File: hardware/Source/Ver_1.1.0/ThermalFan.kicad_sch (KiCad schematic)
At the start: 0 parts

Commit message: update pcb v1.1.0
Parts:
- added C35: 10uF, automative_hexapod:Ceramic_Cap_0805, symbol automative_hexapod:Ceramic_Cap_0805_10uF_16V
- added C36: 100nF, automative_hexapod:Ceramic_Cap_0805, symbol automative_hexapod:Ceramic_Cap_0805_100nF_50V
- added J5: Connector, automative_hexapod:JST-XH-SMD-2-2.54mm, symbol automative_hexapod:JST-XH-SMD-2-2.54mm
- added Q5: LN2302LT1G, automative_hexapod:SOT23, symbol automative_hexapod:LN2302LT1G
- added R36: 4.7Ohm, automative_hexapod:Res_0603, symbol automative_hexapod:Res_4.7_0603_1%
- added R37, R38: 10kOhm, automative_hexapod:Res_0603, symbol automative_hexapod:Res_10K_0603_1%
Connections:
- new net: Q5.1 (G), R36.2, R37.2
- new net: J5.1 (Pin_1), R38.1
- new net: J5.2 (Pin_2), Q5.3 (D)
- new net +5V: C35.2, C36.2, R38.2
- new net BBAI_PWM1A: R36.1
- new net GND: C35.1, C36.1, Q5.2 (S), R37.1
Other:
- note added: "Note: Choose 0R or 10KOhm for R39"
- note added: "Note: Connector for Fan"
- title: (none) -> THERMAL FAN

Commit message: update pcb and schematic
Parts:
- renumbered C35 to C29, C36 to C30, Q5 to Q3, R36 to R38, R37 to R39, R38 to R40
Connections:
- net GND: now also J5.SH (Pin_3)
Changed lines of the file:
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@@
 	(text "Note: Connector for Fan"
 		(exclude_from_sim no)
-		(at 193.548 94.234 0)
+		(at 208.788 94.234 0)
 		(effects
 			(font
@@
 	(text "Note: Choose 0R or 10KOhm for R39"
 		(exclude_from_sim no)
-		(at 187.706 84.328 0)
+		(at 202.946 84.328 0)
 		(effects
 			(font
@@
 	(wire
 		(pts
+			(xy 179.07 97.79) (xy 175.26 97.79)
+		)
+		(stroke
+			(width 0)
+			(type default)
+		)
+	)
+	(wire
+		(pts
 			(xy 92.71 90.17) (xy 111.76 90.17)
 		)
@@
 	(wire
 		(pts
-			(xy 163.83 92.71) (xy 156.21 92.71)
+			(xy 179.07 92.71) (xy 156.21 92.71)
 		)
 		(stroke
@@
 	(wire
 		(pts
+			(xy 175.26 97.79) (xy 175.26 99.06)
+		)
+		(stroke
+			(width 0)
+			(type default)
+		)
+	)
+	(wire
+		(pts
 			(xy 92.71 90.17) (xy 92.71 92.71)
 		)
@@
 	(wire
 		(pts
-			(xy 163.83 95.25) (xy 156.21 95.25)
+			(xy 179.07 95.25) (xy 156.21 95.25)
 		)
 		(stroke
@@
 				(justify right)
 				(hide yes)
+			)
+		)
+	)
+	(symbol
+		(lib_id "power:GND")
+		(at 175.26 99.06 0)
+		(unit 1)
+		(exclude_from_sim no)
+		(in_bom yes)
+		(on_board yes)
+		(dnp no)
+		(fields_autoplaced yes)
+		(property "Reference" "#PWR091"
+			(at 175.26 105.41 0)
+			(effects
+				(font
+					(size 1.27 1.27)
+				)
+				(hide yes)
+			)
+		)
+		(property "Value" "GND"
+			(at 175.26 104.14 0)
+			(effects
+				(font
+					(size 1.27 1.27)
+				)
+			)
+		)
+		(property "Footprint" ""
+			(at 175.26 99.06 0)
+			(effects
+				(font
+					(size 1.27 1.27)
+				)
+				(hide yes)
+			)
+		)
+		(property "Datasheet" ""
+			(at 175.26 99.06 0)
+			(effects
+				(font
+					(size 1.27 1.27)
+				)
+				(hide yes)
+			)
+		)
+		(property "Description" "Power symbol creates a global label with name \"GND\" , ground"
+			(at 175.26 99.06 0)
+			(effects
+				(font
+					(size 1.27 1.27)
+				)
+				(hide yes)
+			)
+		)
+		(pin "1"
+		)
+		(instances
+			(project "Automative_Hexapod"
+				(path "/c07b6013-2147-4cef-a16e-342deb9ccbf5/d11b61d9-d9a4-4f55-b72c-db353535a927"
+					(reference "#PWR091")
+					(unit 1)
+				)
 			)
 		)
@@
 		(on_board yes)
 		(dnp no)
-		(property "Reference" "R36"
+		(property "Reference" "R38"
 			(at 132.08 100.838 0)
 			(effects
@@
 			(project ""
 				(path "/c07b6013-2147-4cef-a16e-342deb9ccbf5/d11b61d9-d9a4-4f55-b72c-db353535a927"
-					(reference "R36")
+					(reference "R38")
 					(unit 1)
 				)
@@
 		(dnp no)
 		(fields_autoplaced yes)
-		(property "Reference" "R38"
+		(property "Reference" "R40"
 			(at 158.75 80.0099 90)
 			(effects
@@
 			(project ""
 				(path "/c07b6013-2147-4cef-a16e-342deb9ccbf5/d11b61d9-d9a4-4f55-b72c-db353535a927"
-					(reference "R38")
+					(reference "R40")
 					(unit 1)
 				)
@@
 		(on_board yes)
 		(dnp no)
-		(property "Reference" "C35"
+		(property "Reference" "C29"
 			(at 85.09 83.82 90)
 			(effects
@@
 			(project "Automative_Hexapod"
 				(path "/c07b6013-2147-4cef-a16e-342deb9ccbf5/d11b61d9-d9a4-4f55-b72c-db353535a927"
-					(reference "C35")
+					(reference "C29")
 					(unit 1)
 				)
@@
 		(dnp no)
 		(fields_autoplaced yes)
-		(property "Reference" "Q5"
+		(property "Reference" "Q3"
 			(at 160.02 102.8699 0)
 			(effects
@@
 			(project "Automative_Hexapod"
 				(path "/c07b6013-2147-4cef-a16e-342deb9ccbf5/d11b61d9-d9a4-4f55-b72c-db353535a927"
-					(reference "Q5")
+					(reference "Q3")
 					(unit 1)
 				)
@@
 		(on_board yes)
 		(dnp no)
-		(property "Reference" "C36"
+		(property "Reference" "C30"
 			(at 104.14 83.82 90)
 			(effects
@@
 			(project "Automative_Hexapod"
 				(path "/c07b6013-2147-4cef-a16e-342deb9ccbf5/d11b61d9-d9a4-4f55-b72c-db353535a927"
-					(reference "C36")
+					(reference "C30")
 					(unit 1)
 				)
@@
 	(symbol
 		(lib_id "automative_hexapod:JST-XH-SMD-2-2.54mm")
-		(at 168.91 92.71 0)
+		(at 184.15 92.71 0)
 		(unit 1)
 		(exclude_from_sim no)
@@
 		(fields_autoplaced yes)
 		(property "Reference" "J5"
-			(at 170.18 90.8049 0)
+			(at 185.42 90.8049 0)
 			(effects
 				(font
@@
 		)
 		(property "Value" "Connector"
-			(at 170.18 93.3449 0)
+			(at 185.42 93.3449 0)
 			(effects
 				(font
@@
 		)
 		(property "Footprint" "automative_hexapod:JST-XH-SMD-2-2.54mm"
-			(at 169.672 101.6 0)
+			(at 184.912 101.6 0)
 			(effects
 				(font
@@
 		)
 		(property "Datasheet" "~"
-			(at 168.91 92.71 0)
+			(at 184.15 92.71 0)
 			(effects
 				(font
@@
 		)
 		(property "Description" "250V 3A"
-			(at 170.942 101.6 0)
+			(at 186.182 101.6 0)
 			(effects
 				(font
@@
 		)
 		(property "Value 2" "~"
-			(at 170.18 95.25 0)
+			(at 185.42 95.25 0)
 			(effects
 				(font
@@
 		)
 		(property "Value 3" "XH2.54mm"
-			(at 170.18 97.1549 0)
+			(at 185.42 97.1549 0)
 			(effects
 				(font
@@
 		)
 		(property "Value 4" "~"
-			(at 168.91 92.71 0)
+			(at 184.15 92.71 0)
 			(effects
 				(font
@@
 		)
 		(property "Supply Name" "Thegioiic"
-			(at 170.942 101.6 0)
+			(at 186.182 101.6 0)
 			(effects
 				(font
@@
 		)
 		(property "Supply Part Number" " Đầu XH2.54mm 2 Chân Dán SMD Nằm Ngang"
-			(at 168.91 101.6 0)
+			(at 184.15 101.6 0)
 			(effects
 				(font
@@
 		)
 		(property "Supply URL" "https://www.Thegioiic.com/dau-xh2-54mm-2-chan-dan-smd-nam-ngang"
-			(at 168.91 101.6 0)
+			(at 184.15 101.6 0)
 			(effects
 				(font
@@
 		)
 		(pin "2"
+		)
+		(pin "SH"
 		)
 		(instances
@@
 		(on_board yes)
 		(dnp no)
-		(property "Reference" "#PWR089"
+		(property "Reference" "#PWR087"
 			(at 92.71 78.74 0)
 			(effects
@@
 			(project "Automative_Hexapod"
 				(path "/c07b6013-2147-4cef-a16e-342deb9ccbf5/d11b61d9-d9a4-4f55-b72c-db353535a927"
-					(reference "#PWR089")
+					(reference "#PWR087")
 					(unit 1)
 				)
@@
 		(on_board yes)
 		(dnp no)
-		(property "Reference" "#PWR092"
+		(property "Reference" "#PWR090"
 			(at 156.21 82.55 0)
 			(effects
@@
 			(project "Automative_Hexapod"
 				(path "/c07b6013-2147-4cef-a16e-342deb9ccbf5/d11b61d9-d9a4-4f55-b72c-db353535a927"
-					(reference "#PWR092")
+					(reference "#PWR090")
 					(unit 1)
 				)
@@
 		(on_board yes)
 		(dnp no)
-		(property "Reference" "R37"
+		(property "Reference" "R39"
 			(at 136.144 113.03 90)
 			(effects
@@
 			(project "Automative_Hexapod"
 				(path "/c07b6013-2147-4cef-a16e-342deb9ccbf5/d11b61d9-d9a4-4f55-b72c-db353535a927"
-					(reference "R37")
+					(reference "R39")
 					(unit 1)
 				)
@@
 		(dnp no)
 		(fields_autoplaced yes)
-		(property "Reference" "#PWR090"
+		(property "Reference" "#PWR088"
 			(at 92.71 99.06 0)
 			(effects
@@
 			(project "Automative_Hexapod"
 				(path "/c07b6013-2147-4cef-a16e-342deb9ccbf5/d11b61d9-d9a4-4f55-b72c-db353535a927"
-					(reference "#PWR090")
+					(reference "#PWR088")
 					(unit 1)
 				)
@@
 		(dnp no)
 		(fields_autoplaced yes)
-		(property "Reference" "#PWR091"
+		(property "Reference" "#PWR089"
 			(at 142.24 129.54 0)
 			(effects
@@
 			(project "Automative_Hexapod"
 				(path "/c07b6013-2147-4cef-a16e-342deb9ccbf5/d11b61d9-d9a4-4f55-b72c-db353535a927"
-					(reference "#PWR091")
+					(reference "#PWR089")
 					(unit 1)
 				)

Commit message: Update PCB_Ver1.1.0
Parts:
- removed R38: 4.7Ohm, automative_hexapod:Res_0603, symbol automative_hexapod:Res_4.7_0603_1%
- added R38: 4.7Ohm, automative_hexapod:Res_0603, symbol automative_hexapod:Res_4.7R_0603_1%
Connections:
- net BBAI_PWM1A: now also R38.1
- net at Q3.1 (G), R39.2: now also R38.2
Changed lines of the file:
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@@
 		(dnp no)
 		(fields_autoplaced yes)
-		(property "Reference" "#PWR091"
+		(property "Reference" "#PWR092"
 			(at 175.26 105.41 0)
 			(effects
@@
 			(project "Automative_Hexapod"
 				(path "/c07b6013-2147-4cef-a16e-342deb9ccbf5/d11b61d9-d9a4-4f55-b72c-db353535a927"
-					(reference "#PWR091")
-					(unit 1)
-				)
-			)
-		)
-	)
-	(symbol
-		(lib_id "automative_hexapod:Res_4.7_0603_1%")
-		(at 132.08 104.14 0)
-		(unit 1)
-		(exclude_from_sim no)
-		(in_bom yes)
-		(on_board yes)
-		(dnp no)
-		(property "Reference" "R38"
-			(at 132.08 100.838 0)
-			(effects
-				(font
-					(size 1.27 1.27)
-				)
-			)
-		)
-		(property "Value" "4.7Ohm"
-			(at 132.08 107.442 0)
-			(effects
-				(font
-					(size 1.27 1.27)
-				)
-			)
-		)
-		(property "Footprint" "automative_hexapod:Res_0603"
-			(at 131.826 99.06 0)
-			(effects
-				(font
-					(size 1.27 1.27)
-				)
-				(hide yes)
-			)
-		)
-		(property "Datasheet" ""
-			(at 132.08 101.6 0)
-			(effects
-				(font
-					(size 1.27 1.27)
-				)
-				(hide yes)
-			)
-		)
-		(property "Description" "Res_4.7_0603_1%"
-			(at 131.572 99.314 0)
-			(effects
-				(font
-					(size 1.27 1.27)
-				)
-				(hide yes)
-			)
-		)
-		(property "Value 2" "1/10W"
-			(at 132.08 109.982 0)
-			(effects
-				(font
-					(size 1.27 1.27)
-					(color 0 132 132 1)
-				)
-			)
-		)
-		(property "Value 3" "0603"
-			(at 132.08 112.522 0)
-			(effects
-				(font
-					(size 1.27 1.27)
-					(color 0 132 132 1)
-				)
-			)
-		)
-		(property "Value 4" "1%"
-			(at 132.08 115.062 0)
-			(effects
-				(font
-					(size 1.27 1.27)
-					(color 0 132 132 1)
-				)
-			)
-		)
-		(property "Supply Name" "Thegioiic"
-			(at 132.334 99.314 0)
-			(effects
-				(font
-					(size 1.27 1.27)
-				)
-				(hide yes)
-			)
-		)
-		(property "Supply Part Number" "Điện Trở 4.7 Ohm 0603 1%"
-			(at 132.334 99.314 0)
-			(effects
-				(font
-					(size 1.27 1.27)
-				)
-				(hide yes)
-			)
-		)
-		(property "Supply URL" "https://www.Thegioiic.com/dien-tro-4-7-ohm-0603-1-"
-			(at 131.826 99.568 0)
-			(effects
-				(font
-					(size 1.27 1.27)
-				)
-				(hide yes)
-			)
-		)
-		(pin "1"
-		)
-		(pin "2"
-		)
-		(instances
-			(project ""
-				(path "/c07b6013-2147-4cef-a16e-342deb9ccbf5/d11b61d9-d9a4-4f55-b72c-db353535a927"
-					(reference "R38")
+					(reference "#PWR092")
 					(unit 1)
 				)
@@
 	)
 	(symbol
+		(lib_id "automative_hexapod:Res_4.7R_0603_1%")
+		(at 132.08 104.14 0)
+		(unit 1)
+		(exclude_from_sim no)
+		(in_bom yes)
+		(on_board yes)
+		(dnp no)
+		(property "Reference" "R38"
+			(at 132.08 101.6 0)
+			(effects
+				(font
+					(size 1.27 1.27)
+				)
+			)
+		)
+		(property "Value" "4.7Ohm"
+			(at 132.08 107.188 0)
+			(effects
+				(font
+					(size 1.27 1.27)
+				)
+			)
+		)
+		(property "Footprint" "automative_hexapod:Res_0603"
+			(at 131.826 99.06 0)
+			(effects
+				(font
+					(size 1.27 1.27)
+				)
+				(hide yes)
+			)
+		)
+		(property "Datasheet" ""
+			(at 132.08 101.6 0)
+			(effects
+				(font
+					(size 1.27 1.27)
+				)
+				(hide yes)
+			)
+		)
+		(property "Description" "Res_4.7R_0603_1%"
+			(at 131.572 99.314 0)
+			(effects
+				(font
+					(size 1.27 1.27)
+				)
+				(hide yes)
+			)
+		)
+		(property "Value 2" "1/10W"
+			(at 132.08 109.728 0)
+			(effects
+				(font
+					(size 1.27 1.27)
+					(color 0 132 132 1)
+				)
+			)
+		)
+		(property "Value 3" "0603"
+			(at 132.08 112.268 0)
+			(effects
+				(font
+					(size 1.27 1.27)
+					(color 0 132 132 1)
+				)
+			)
+		)
+		(property "Value 4" "1%"
+			(at 132.08 114.808 0)
+			(effects
+				(font
+					(size 1.27 1.27)
+					(color 0 132 132 1)
+				)
+			)
+		)
+		(property "Supply Name" "Thegioiic"
+			(at 132.334 99.314 0)
+			(effects
+				(font
+					(size 1.27 1.27)
+				)
+				(hide yes)
+			)
+		)
+		(property "Supply Part Number" "Điện Trở 4.7 Ohm 0603 1%"
+			(at 132.334 99.314 0)
+			(effects
+				(font
+					(size 1.27 1.27)
+				)
+				(hide yes)
+			)
+		)
+		(property "Supply URL" "https://www.Thegioiic.com/dien-tro-4-7-ohm-0603-1-"
+			(at 131.826 99.568 0)
+			(effects
+				(font
+					(size 1.27 1.27)
+				)
+				(hide yes)
+			)
+		)
+		(pin "2"
+		)
+		(pin "1"
+		)
+		(instances
+			(project ""
+				(path "/c07b6013-2147-4cef-a16e-342deb9ccbf5/d11b61d9-d9a4-4f55-b72c-db353535a927"
+					(reference "R38")
+					(unit 1)
+				)
+			)
+		)
+	)
+	(symbol
 		(lib_id "automative_hexapod:LN2302LT1G")
 		(at 156.21 104.14 0)
@@
 		(on_board yes)
 		(dnp no)
-		(property "Reference" "#PWR087"
+		(property "Reference" "#PWR088"
 			(at 92.71 78.74 0)
 			(effects
@@
 			(project "Automative_Hexapod"
 				(path "/c07b6013-2147-4cef-a16e-342deb9ccbf5/d11b61d9-d9a4-4f55-b72c-db353535a927"
-					(reference "#PWR087")
+					(reference "#PWR088")
 					(unit 1)
 				)
@@
 		(on_board yes)
 		(dnp no)
-		(property "Reference" "#PWR090"
+		(property "Reference" "#PWR091"
 			(at 156.21 82.55 0)
 			(effects
@@
 			(project "Automative_Hexapod"
 				(path "/c07b6013-2147-4cef-a16e-342deb9ccbf5/d11b61d9-d9a4-4f55-b72c-db353535a927"
-					(reference "#PWR090")
+					(reference "#PWR091")
 					(unit 1)
 				)
@@
 		(dnp no)
 		(fields_autoplaced yes)
-		(property "Reference" "#PWR088"
+		(property "Reference" "#PWR089"
 			(at 92.71 99.06 0)
 			(effects
@@
 			(project "Automative_Hexapod"
 				(path "/c07b6013-2147-4cef-a16e-342deb9ccbf5/d11b61d9-d9a4-4f55-b72c-db353535a927"
-					(reference "#PWR088")
+					(reference "#PWR089")
 					(unit 1)
 				)
@@
 		(dnp no)
 		(fields_autoplaced yes)
-		(property "Reference" "#PWR089"
+		(property "Reference" "#PWR090"
 			(at 142.24 129.54 0)
 			(effects
@@
 			(project "Automative_Hexapod"
 				(path "/c07b6013-2147-4cef-a16e-342deb9ccbf5/d11b61d9-d9a4-4f55-b72c-db353535a927"
-					(reference "#PWR089")
+					(reference "#PWR090")
 					(unit 1)
 				)

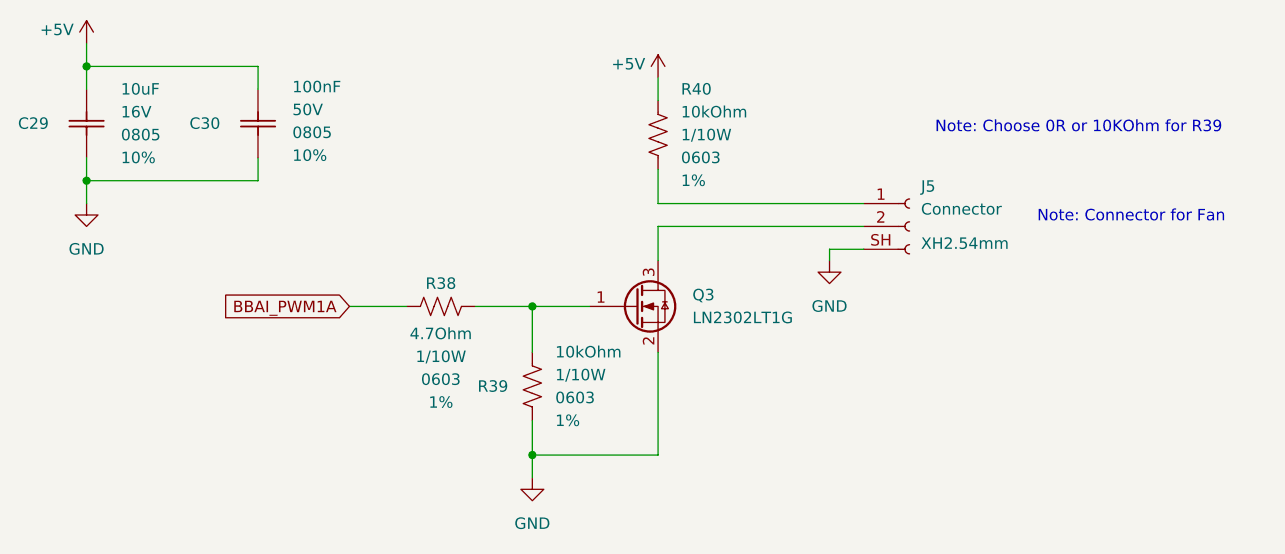
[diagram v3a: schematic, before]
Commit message: Generate PDF Schematic Ver1.1.0 and add README.md
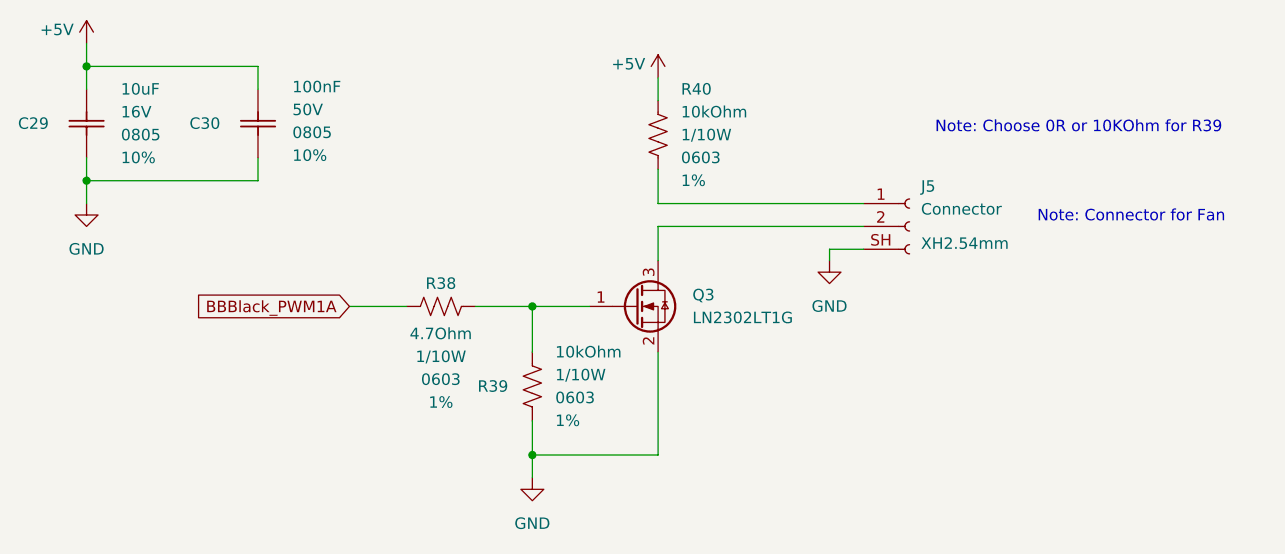
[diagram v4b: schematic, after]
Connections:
- net BBAI_PWM1A renamed BBBlack_PWM1A
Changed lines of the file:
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@@
 		)
 	)
-	(global_label "BBAI_PWM1A"
+	(global_label "BBBlack_PWM1A"
 		(shape input)
 		(at 121.92 104.14 180)
